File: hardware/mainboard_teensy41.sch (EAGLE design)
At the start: 189 parts, among them IC1 ATMEGA328-20P, IC2 7805TV, Q1 2N3904, Q2 2N3904, Q3 2N3904, Q4 2N3904, Q5 2N3904, Q6 2N3904

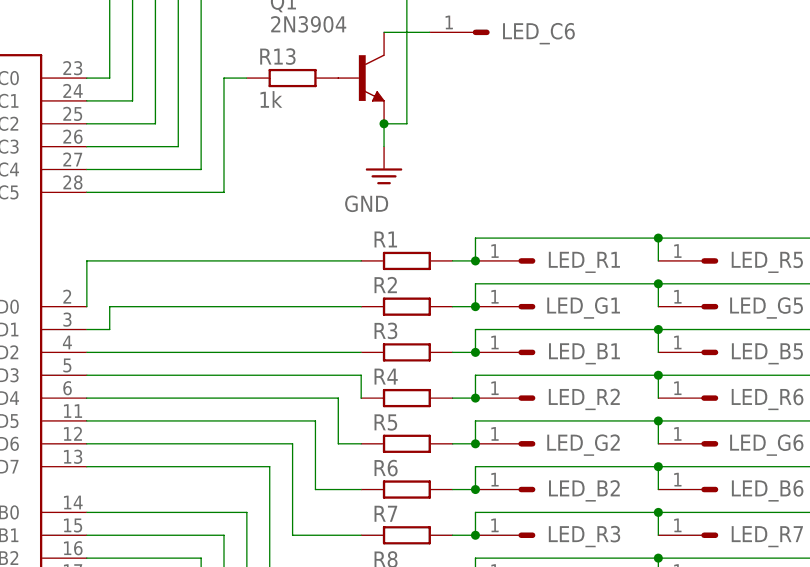
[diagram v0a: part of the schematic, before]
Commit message: Created custom SPISlave class to use 2 pins only
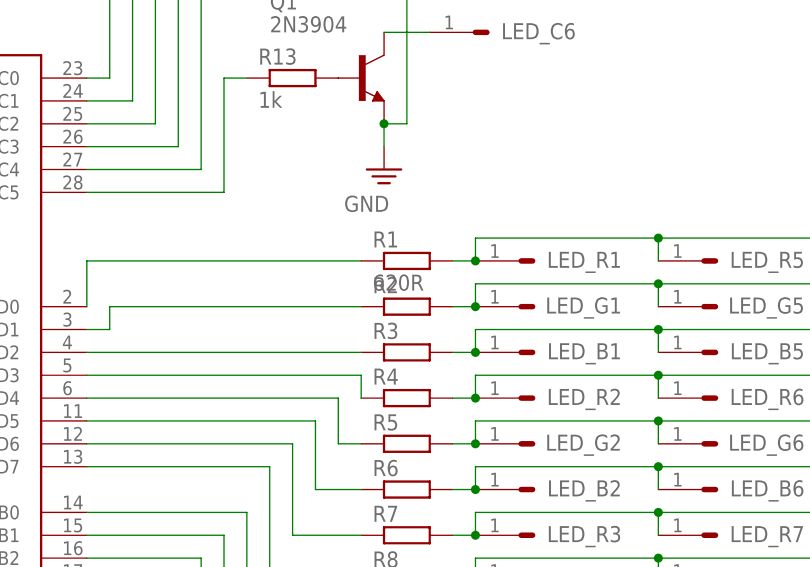
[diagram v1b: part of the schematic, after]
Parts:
- R1: value (none) -> 620R
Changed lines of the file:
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@@
 </part>
 <part name="IC1" library="atmega328" deviceset="ATMEGA328*P" device="" technology="-20"/>
-<part name="R1" library="resistors" deviceset="RESISTOR" device="RESISTOR/UPRIGHT/7.5"/>
+<part name="R1" library="resistors" deviceset="RESISTOR" device="RESISTOR/UPRIGHT/7.5" value="620R"/>
 <part name="R2" library="resistors" deviceset="RESISTOR" device="RESISTOR/UPRIGHT/7.5"/>
 <part name="R3" library="resistors" deviceset="RESISTOR" device="RESISTOR/UPRIGHT/7.5"/>

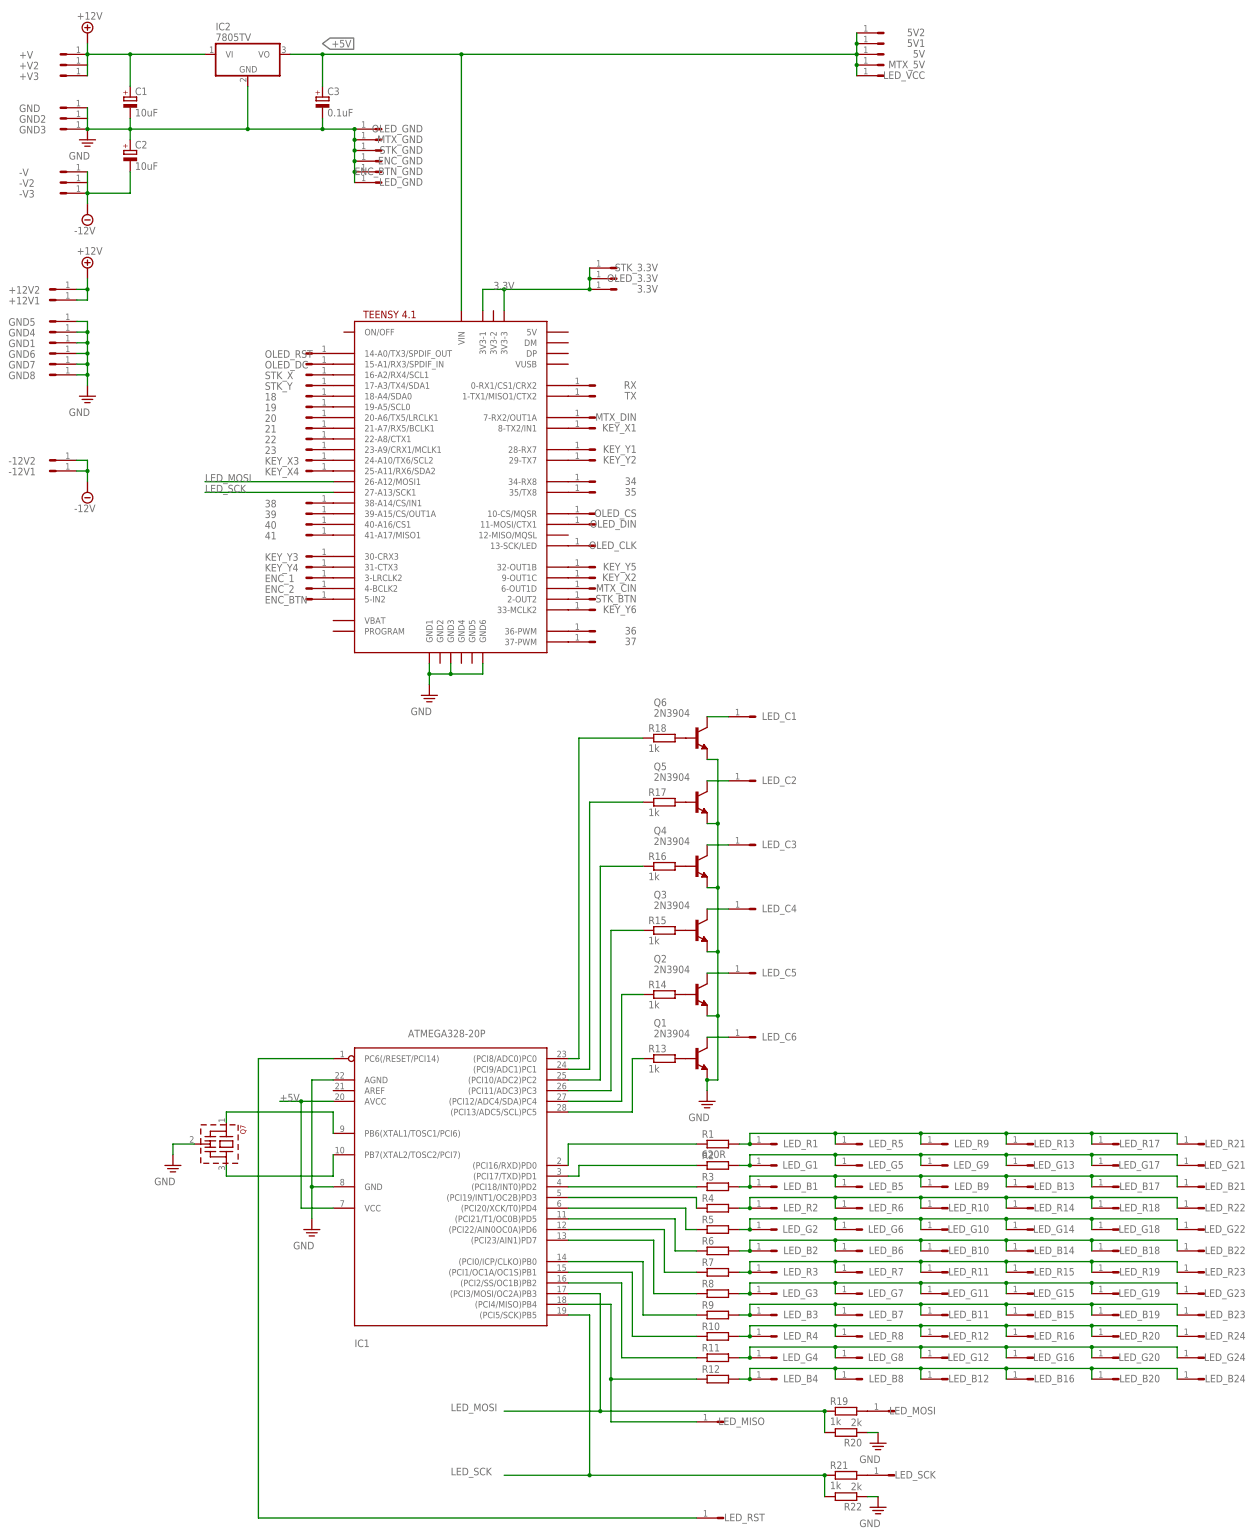
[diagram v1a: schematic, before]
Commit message: Use serial to communicate with keyboard led driver
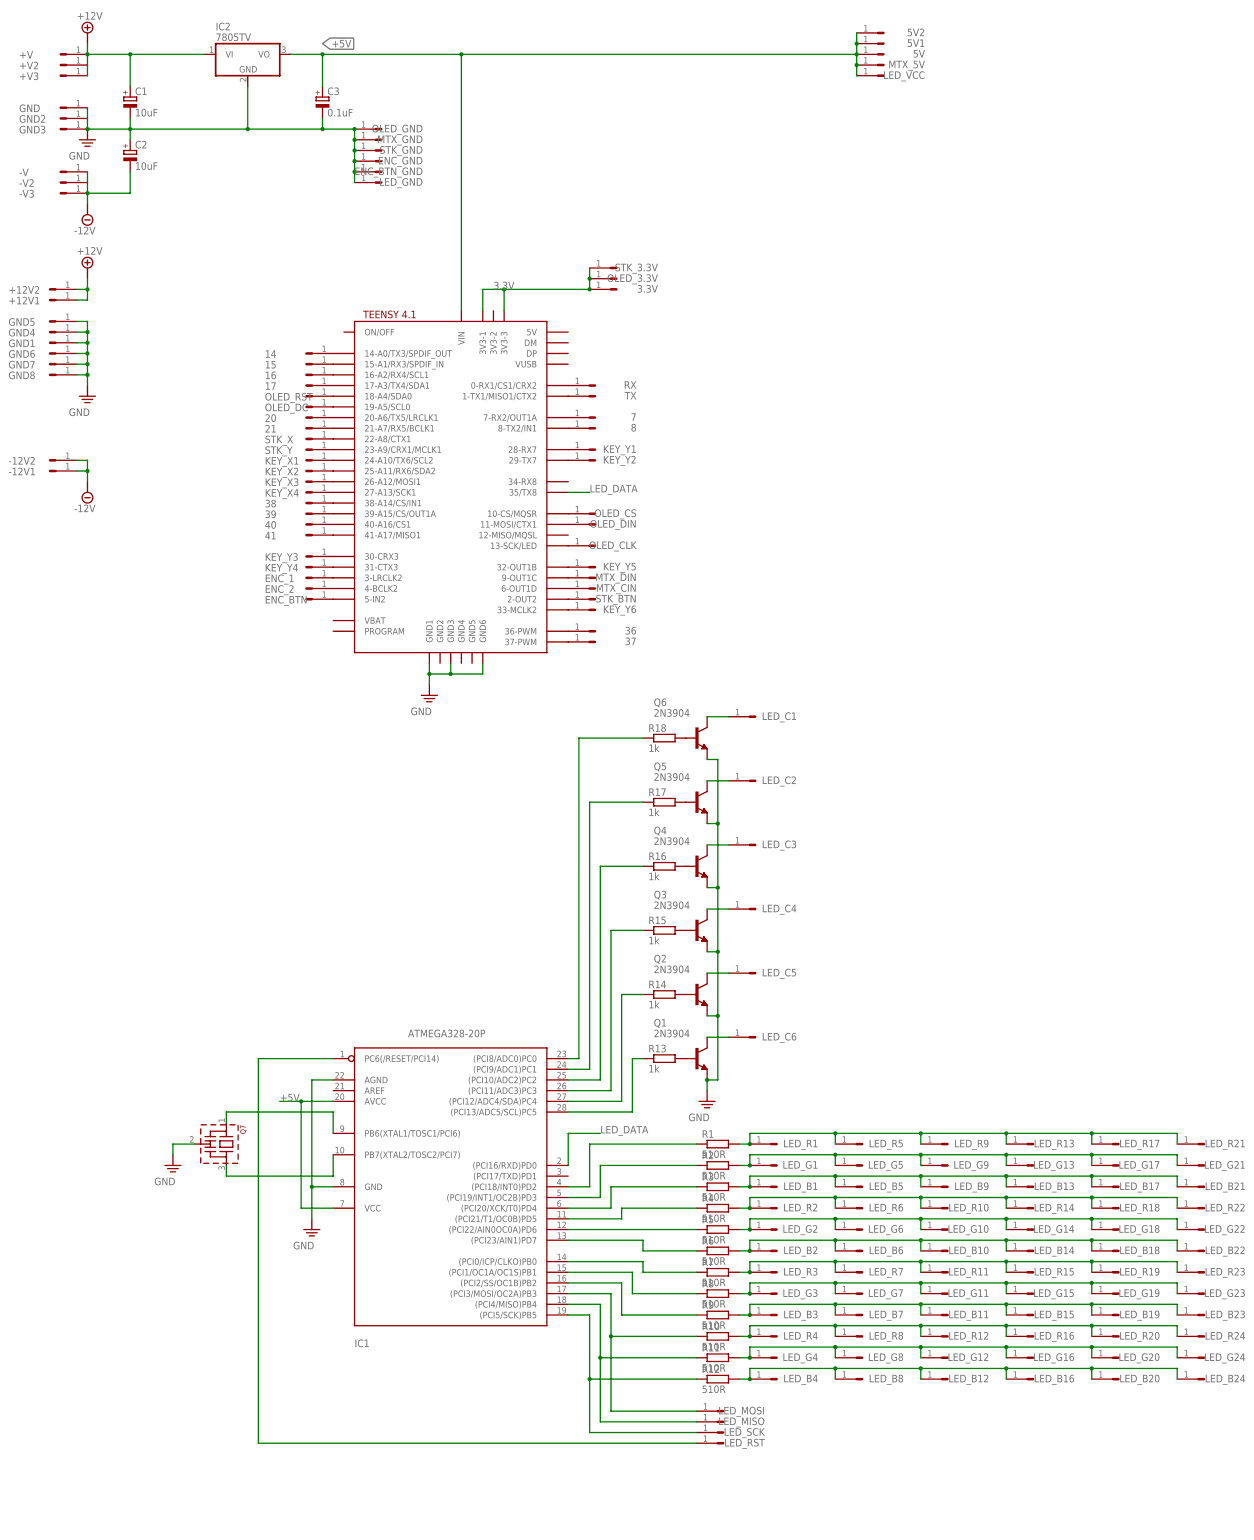
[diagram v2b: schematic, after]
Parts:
- removed 18, 19, 22, 23, 34, 35: HEADER/MALE/01, connectors:HEADER/MALE/01
- removed R19, R21: 1k, resistors:RESISTORRESISTOR/UPRIGHT/7.5
- removed R20, R22: 2k, resistors:RESISTORRESISTOR/UPRIGHT/7.5
- added 14, 15, 16, 17, 7, 8: HEADER/MALE/01, connectors:HEADER/MALE/01
- R1: value 620R -> 510R
- R10, R11, R12, R2, R3, R4, R5, R6, R7, R8, R9: value (none) -> 510R
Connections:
- removed net LED_MOSI: IC1.(PCI3/MOSI/OC2A)PB3, R19.1, R20.2, U$1.26-A12/MOSI1
- removed net LED_SCK: IC1.(PCI5/SCK)PB5, R21.1, R22.2, U$1.27-A13/SCK1
- removed net N$78: 23.3, U$1.23-A9/CRX1/MCLK1
- removed net N$85: LED_MOSI.3, R19.2
- new net LED_DATA: IC1.(PCI16/RXD)PD0, U$1.35/TX8
- net GND: no longer R20.1, R22.1
- net N$1: now also IC1.(PCI18/INT0)PD2; no longer IC1.(PCI16/RXD)PD0
- net N$12: now also KEY_X3.3, U$1.26-A12/MOSI1; no longer KEY_X2.3, U$1.9-OUT1C
- net N$21: now also U$1.27-A13/SCK1; no longer U$1.25-A11/RX6/SDA2
- net N$22: now also STK_X.3, U$1.22-A8/CTX1; no longer KEY_X3.3, U$1.24-A10/TX6/SCL2
- net N$23: now also U$1.23-A9/CRX1/MCLK1; no longer U$1.17-A3/TX4/SDA1
- net N$24: now also OLED_RST.3, U$1.18-A4/SDA0; no longer STK_X.3, U$1.16-A2/RX4/SCL1
- net N$25: now also U$1.19-A5/SCL0; no longer U$1.15-A1/RX3/SPDIF_IN
- net N$26: now also 14.3; no longer OLED_RST.3
- net N$27: now also IC1.(PCI19/INT1/OC2B)PD3; no longer IC1.(PCI17/TXD)PD1
- net N$28: now also IC1.(PCI20/XCK/T0)PD4; no longer IC1.(PCI18/INT0)PD2
- net N$29: now also IC1.(PCI21/T1/OC0B)PD5; no longer IC1.(PCI19/INT1/OC2B)PD3
- net N$30: now also IC1.(PCI22/AIN0OC0A)PD6; no longer IC1.(PCI20/XCK/T0)PD4
- net N$31: now also IC1.(PCI23/AIN1)PD7; no longer IC1.(PCI21/T1/OC0B)PD5
- net N$32: now also IC1.(PCI0/ICP/CLKO)PB0; no longer IC1.(PCI22/AIN0OC0A)PD6
- net N$33: now also IC1.(PCI1/OC1A/OC1S)PB1; no longer IC1.(PCI23/AIN1)PD7
- net N$34: now also IC1.(PCI2/SS/OC1B)PB2; no longer IC1.(PCI0/ICP/CLKO)PB0
- net N$35: now also IC1.(PCI3/MOSI/OC2A)PB3, LED_MOSI.3; no longer IC1.(PCI1/OC1A/OC1S)PB1
- net N$36: now also IC1.(PCI4/MISO)PB4, LED_MISO.3; no longer IC1.(PCI2/SS/OC1B)PB2
- net N$37: now also 15.3, U$1.15-A1/RX3/SPDIF_IN; no longer IC1.(PCI4/MISO)PB4, LED_MISO.3, R12.1
- net N$7: now also KEY_X1.3, U$1.24-A10/TX6/SCL2; no longer MTX_DIN.3, U$1.7-RX2/OUT1A
- net N$71: now also 16.3, U$1.16-A2/RX4/SCL1; no longer 34.3, U$1.34-RX8
- net N$72: now also 17.3, U$1.17-A3/TX4/SDA1; no longer 35.3, U$1.35/TX8
- net N$73: now also 7.3, U$1.7-RX2/OUT1A; no longer 18.3, U$1.18-A4/SDA0
- net N$74: now also 8.3, U$1.8-TX2/IN1; no longer 19.3, U$1.19-A5/SCL0
- net N$77: now also MTX_DIN.3, U$1.9-OUT1C; no longer 22.3, U$1.22-A8/CTX1
- net N$8: now also KEY_X2.3, U$1.25-A11/RX6/SDA2; no longer KEY_X1.3, U$1.8-TX2/IN1
- net N$86: now also IC1.(PCI5/SCK)PB5, R12.1; no longer R21.2
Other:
- moved on the sheet: KEY_X1, KEY_X2, KEY_X3, KEY_X4, LED_MOSI, LED_RST, LED_SCK, MTX_DIN, OLED_DC, OLED_RST, STK_X, STK_Y
